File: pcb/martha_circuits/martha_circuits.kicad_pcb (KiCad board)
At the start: 2 copper layers, 115 x 129 mm, 35 parts, among them J1 Conn_01x06, J2 Conn_01x06, J3 Conn_01x06, J4 Conn_01x06, J5 Battery, J6 IMU, Q1 IRF4905, SW1 SW_SPST, U5 LM339

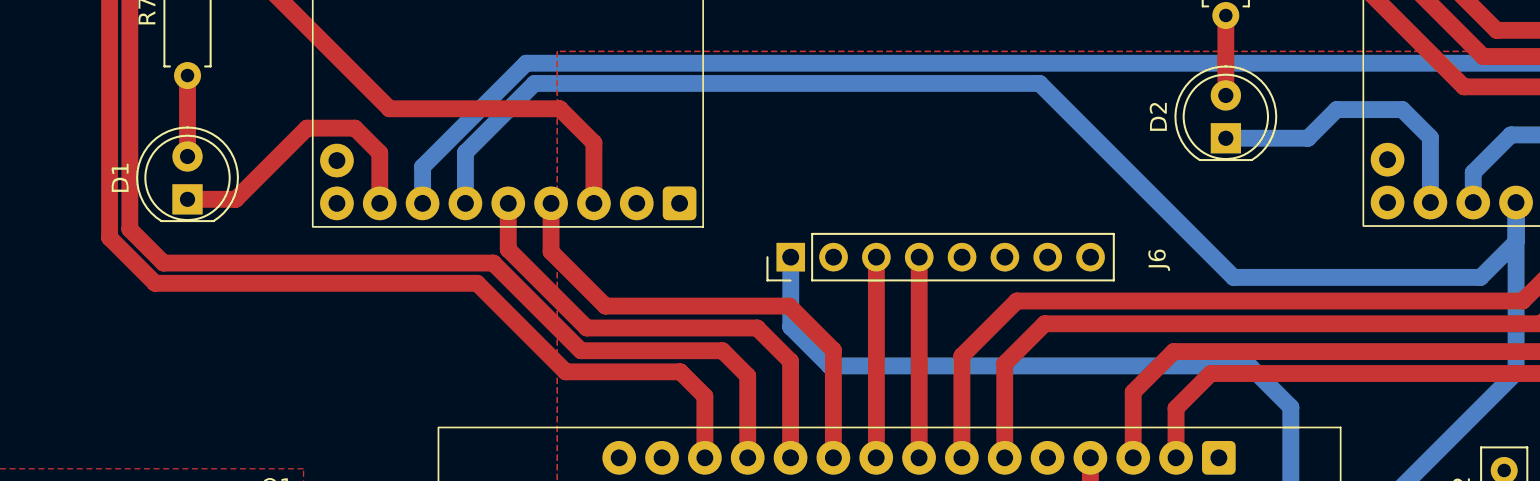
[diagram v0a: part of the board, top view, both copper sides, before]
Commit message: Keep exploration alive across the curriculum and push harder on clearance
The run declined sharply once the curriculum hardened the goals at episode
2400 (medium) and 3600 (hard). Two things compounded: out_of_bounds rose from
~20% to ~50% on the longer routes, and exploration had already annealed away by
then. The entropy/std schedule runs on PPO updates while the curriculum runs on
episodes, and the two were misaligned: the hard phase begins near update 515
but the schedule had the learned std down to ~0.24 and entropy negative there,
so the agent met the harder goals with almost no exploration left and stalled.

Align exploration with the curriculum and settle on a useful floor instead of
near-determinism:
- policy_std_final 0.15 -> 0.25 and entropy_final_fraction 0.15 -> 0.30, so a
  meaningful amount of exploration survives to the end of the run
- entropy_decay_updates 600 -> 1000, so the anneal reaches its floor around
  update 1200, well past the curriculum's hard phase (~update 515) and its end
  (~update 626); the std ceiling is now ~0.35 at the hard transition instead of
  ~0.24

Also raise laser_penalty_scale 0.03 -> 0.05: at 0.03 the last run still hit ~50%
out_of_bounds on the long routes, though that was confounded by the collapsed
exploration, so a stronger clearance gradient plus live exploration should let
the policy actually learn to keep its distance on longer paths.

This changes the reward and exploration landscape the value function is trained
against, so it is meant for a fresh run, not a resume.

Test suite in the ros2_humble container: 175 passed. The 2 remaining failures
in test_shared_training predate this work.

Co-Authored-By: Claude Opus 4.8 <noreply@anthropic.com>
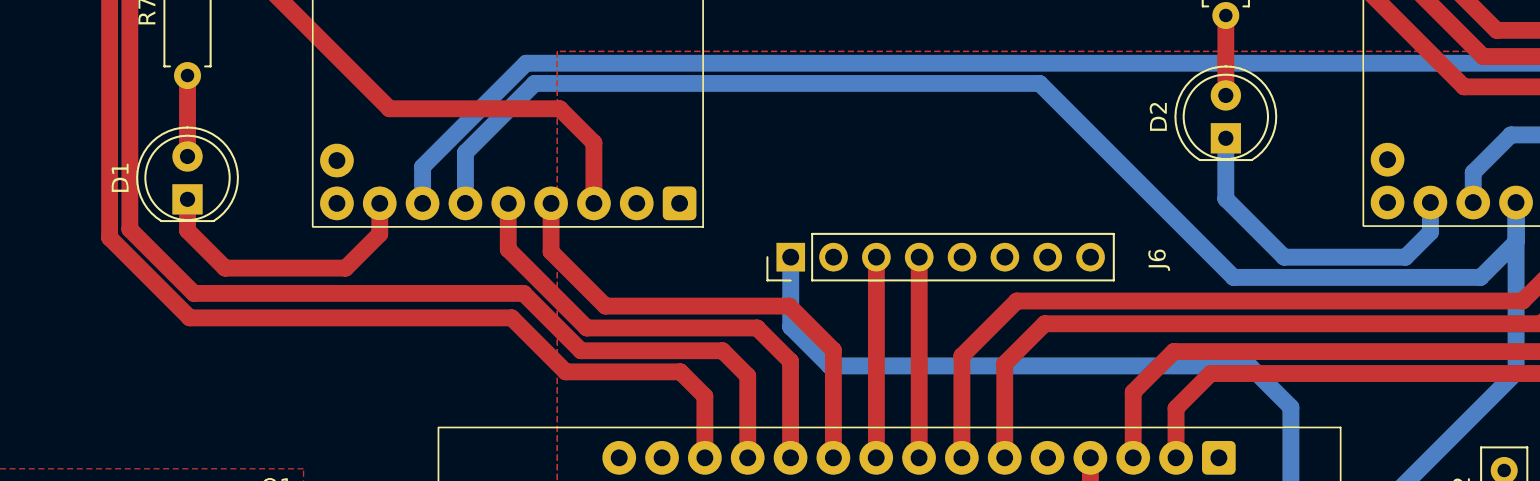
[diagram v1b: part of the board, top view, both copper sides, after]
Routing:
- net FAULT2: track 17.4 -> 19.5 mm

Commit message: Learn obstacle avoidance: drop the OOB death, dense penalty, mastery curriculum
The policy plateaued on medium/long goals and out_of_bounds stayed high because
it was never actually learning to avoid obstacles. Three coupled causes, each
addressed here.

1. out_of_bounds was terminal at the 0.45 m inflated clearance, so the robot
   died the moment it entered the band, ~0.2 m before its 0.58x0.41 m footprint
   could touch anything. It never experienced getting close and recovering, so
   avoidance was learned only from sparse terminal deaths. out_of_bounds is no
   longer terminal: only a real bumper contact (or goal/timeout/stagnation) ends
   an episode. In the band the geodesic distance is undefined, so the last
   finite distance is frozen to keep shaping bounded; out_of_bounds is retained
   in the info dict purely as a near-obstacle diagnostic.

2. The clearance penalty was tiny and linear, negligible against the terminal.
   It is now the main obstacle signal: zero at 0.65 m and growing quadratically
   to laser_penalty_scale (0.10) at contact, so passing close is cheap
   (-0.005/step at 0.5 m) while nearly touching is strongly discouraged
   (-0.07/step at 0.1 m). Combined with removing the OOB death, the policy can
   now learn to thread close without touching.

3. The curriculum advanced on fixed episode fractions, outpacing avoidance, so
   the goals hardened before the policy was ready. CurriculumScheduler now
   raises the distance ceiling by mastery: it advances only when the rolling
   success over a full window clears curriculum_success_threshold (0.55), with a
   per-level episode cap as a stall fallback. curriculum_easy/medium/full_fraction
   are replaced by curriculum_success_threshold/window/min_episodes/max_episodes.

Test suite in the ros2_humble container: 178 passed. The 2 remaining failures
in test_shared_training predate this work.

Co-Authored-By: Claude Opus 4.8 <noreply@anthropic.com>
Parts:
- J5: value Battery -> Conn_01x02_Dean
- R10, R7, R8, R9: value R -> 1k
- moved J5 1.95 mm to (53.0, 111.0)
- moved Q1 1.95 mm to (64.3, 102.3)
- moved R1 1.95 mm to (64.3, 119.7)
- moved SW1 1.95 mm to (53.0, 102.3)
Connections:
- U0 pad 15: +5V -> unconnected-(U0-VIN-Pad15)
